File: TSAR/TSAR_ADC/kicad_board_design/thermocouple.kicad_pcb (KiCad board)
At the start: 4 copper layers, 90.2 x 73.7 mm, 117 parts, among them P1 CONN_02X13, P2 Phoenix 1984756 Terminal Block, U1 LTC3260, U10 MCP3424T-E/ST, U2 LM78L05ACZ_NOPB, U3 AD8495, U4 AD8495, U5 AD8495, U6 AD8495, U7 ADA4062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

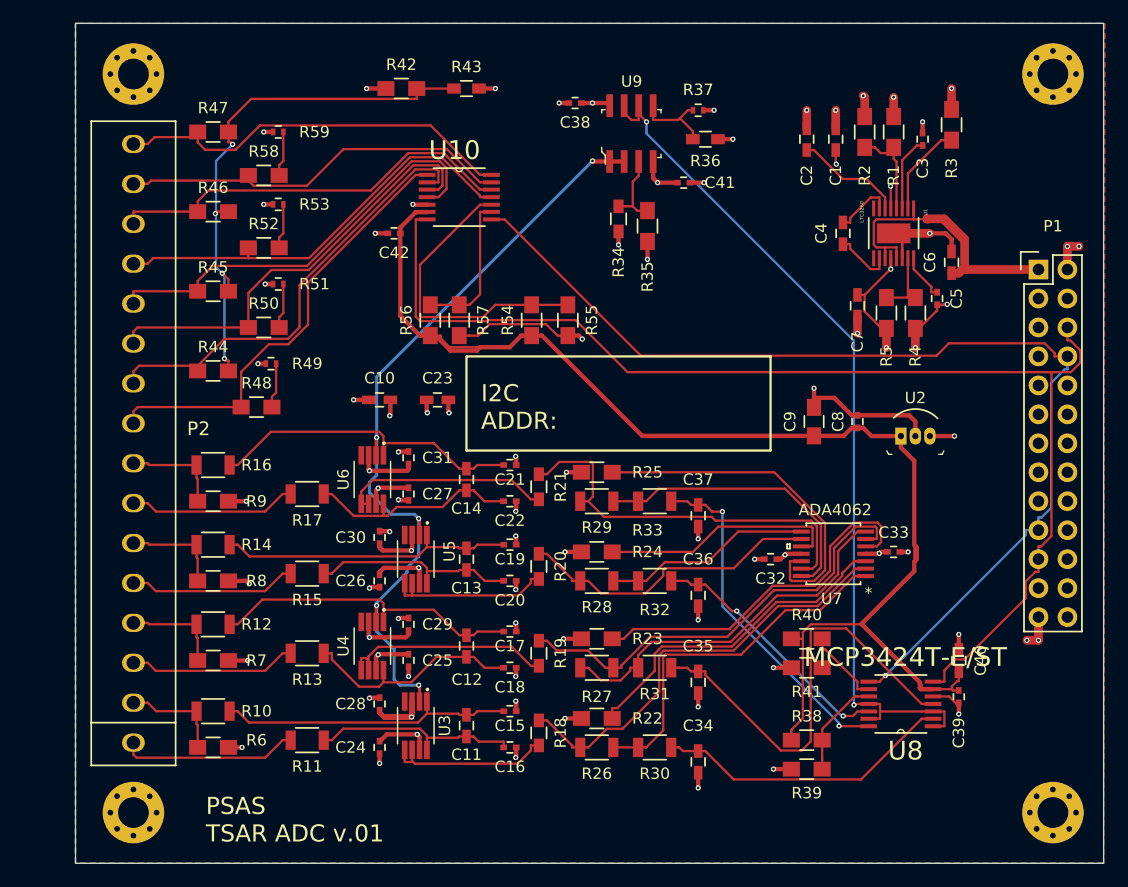
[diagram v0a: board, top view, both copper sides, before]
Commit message: Change from screw terminal block to DB-25.
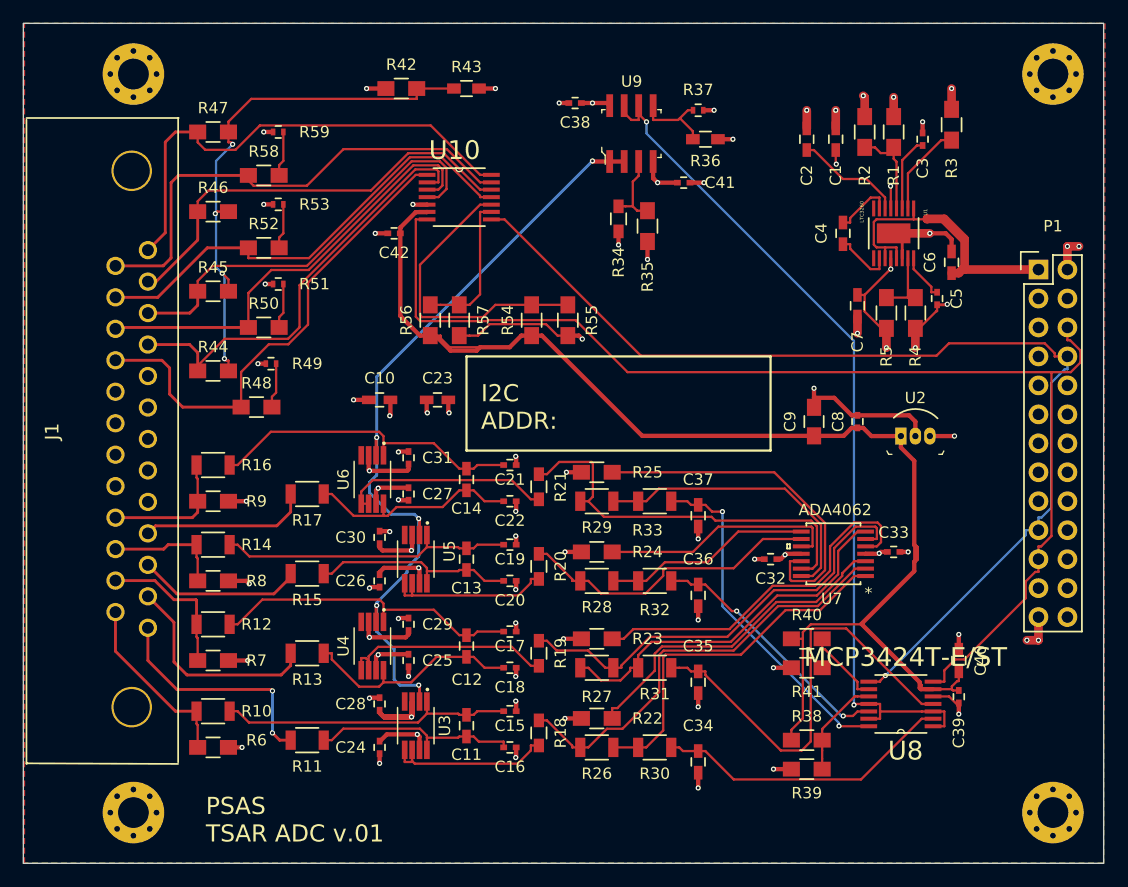
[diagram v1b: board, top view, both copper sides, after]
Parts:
- removed P2: Phoenix 1984756 Terminal Block, snapEda:1984756_phoenix_16_pos_terminal_block
- added J1: DB25, snapEda:TE_Conn_5747846_4_DB25, F.Cu at (83.2, 101.2)
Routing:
- net /pressure_ckt/DiffChan_4+: track 34.7 -> 43.3 mm
- net /pressure_ckt/DiffChan_4-: track 35.5 -> 42.9 mm
- net /thermocouple_ckt/TC_1-: track 9.06 -> 15.9 mm
- net /thermocouple_ckt/TC_1+: track 15.6 -> 20.4 mm, vias 0 -> 2
- net /thermocouple_ckt/TC_2-: track 8.80 -> 13.1 mm
- net /thermocouple_ckt/TC_2+: track 14.7 -> 18.8 mm
- net /pressure_ckt/DiffChan_1+: track 39.4 -> 42.8 mm
- net /pressure_ckt/DiffChan_3+: track 37.7 -> 40.9 mm
- net /thermocouple_ckt/TC_4-: track 8.82 -> 11.6 mm
- net /thermocouple_ckt/TC_3-: track 8.81 -> 10.5 mm
- net /pressure_ckt/DiffChan_3-: track 36.4 -> 38.1 mm
- net /pressure_ckt/DiffChan_2-: track 37.9 -> 37.0 mm
- net /pressure_ckt/DiffChan_1-: track 39.8 -> 39.2 mm
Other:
- board size 90.2 x 73.7 mm -> 94.7 x 73.7 mm

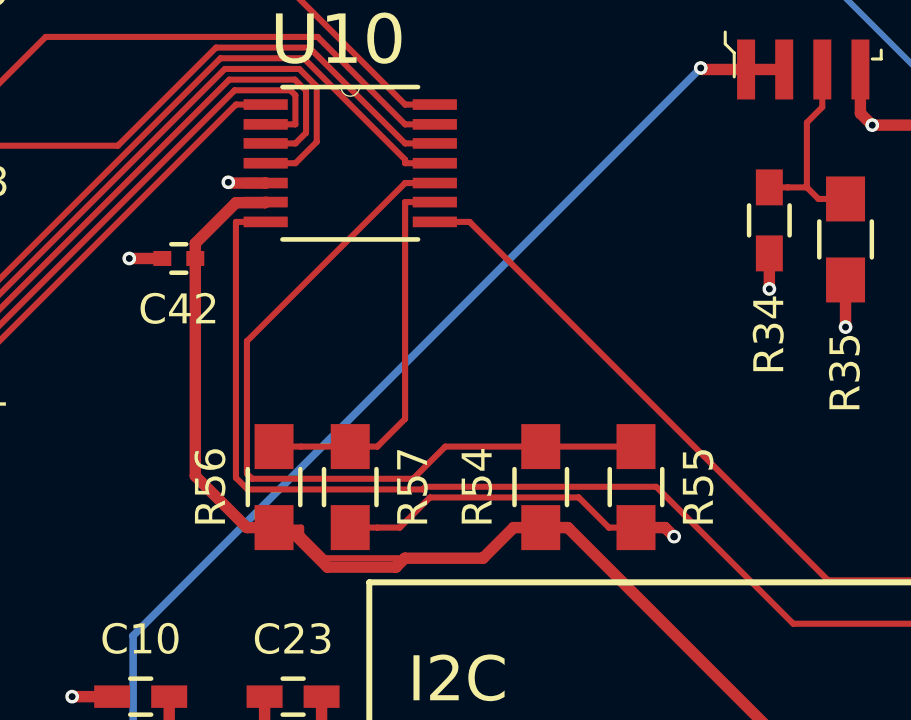
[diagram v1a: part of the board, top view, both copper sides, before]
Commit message: Simplify thermocouple signal chain for better worst case.
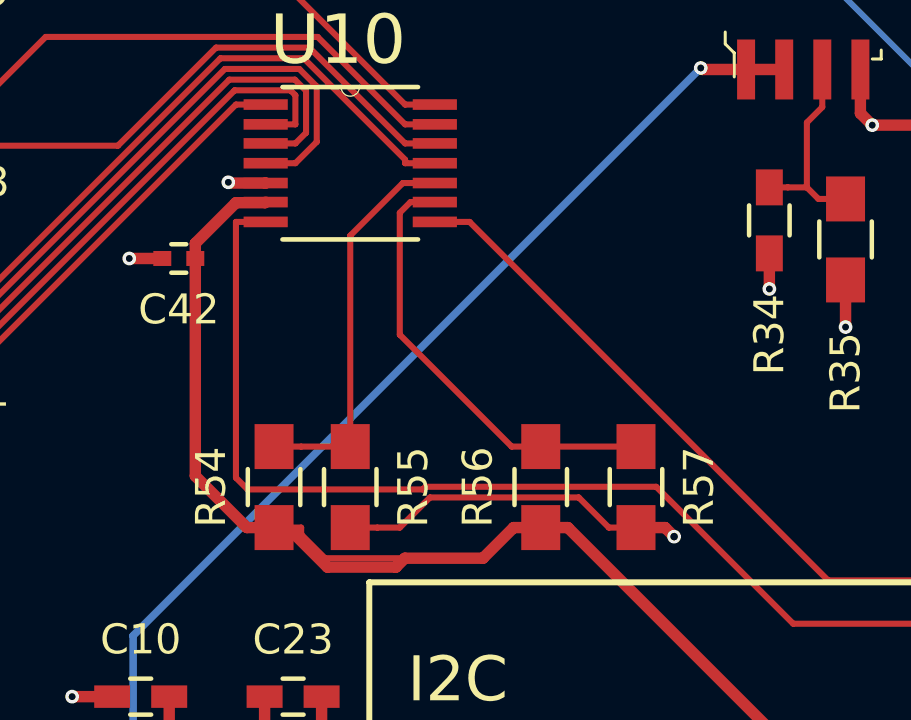
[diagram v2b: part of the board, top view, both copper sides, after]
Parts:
- moved R55 9.53 mm to (110.5, 90.8)
- moved R57 9.53 mm to (120.0, 90.8)
- moved R54 8.89 mm to (108.0, 90.8)
- moved R56 8.89 mm to (116.8, 90.8)
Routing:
- net /pressure_ckt/ADR1: track 26.3 -> 13.1 mm
- net /pressure_ckt/ADR0: track 13.0 -> 14.8 mm

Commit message: Incorporate review comments.  Improve U1 routing, general schematic comments.
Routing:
- net Net-(R4-Pad2): track 5.99 -> 9.11 mm, vias 0 -> 2
- net /power/-10V: track 101.5 -> 103.4 mm, vias 11 -> 13
- net /power/+12V: track 77.9 -> 78.6 mm
- net Net-(C5-Pad1): track 4.13 -> 4.76 mm, vias 0 -> 2
- net /power/+10V: track 41.1 -> 41.0 mm, vias 12 -> 14
